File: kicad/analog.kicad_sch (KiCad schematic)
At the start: 61 parts, among them U1 MP2672GD-0000-Z, U3 MP2236CGJ-Z, U5 MP2672GD-0000-Z, U6 MP2236CGJ-P, U7 MP2236CGJ-P

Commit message: delete trailing space
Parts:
- U1: LCSC PN (none) -> C2837210; LCSC PN  C2837210 -> (none)
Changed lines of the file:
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@@
 			)
 		)
-		(property "LCSC PN " "C2837210"
+		(property "LCSC PN" "C2837210"
 			(at 180.848 27.178 0)
 			(effects

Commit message: update anotations
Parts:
- removed C1, C4, C5, C6, C9: 22u, Capacitor_SMD:C_0402_1005Metric, symbol Device:C
- removed C12, C13, C17, C18, C19, C22: 22u, Capacitor_SMD:C_0805_2012Metric, symbol Device:C
- removed C14: 1u, Capacitor_SMD:C_0805_2012Metric, symbol Device:C
- removed C15, C23: 1u, Capacitor_SMD:C_0603_1608Metric, symbol Device:C
- removed C16: 0.1u, Capacitor_SMD:C_0603_1608Metric, symbol Device:C
- removed C2: 220p, Capacitor_SMD:C_0402_1005Metric, symbol Device:C
- removed C20: 220p, Capacitor_SMD:C_0603_1608Metric, symbol Device:C
- removed C21: 10u, Capacitor_SMD:C_0805_2012Metric, symbol Device:C
- removed C25: 22u, Capacitor_SMD:C_1206_3216Metric, symbol Device:C
- removed C26: 100n, Capacitor_SMD:C_0603_1608Metric, symbol Device:C
- removed C3: 0.1u, Capacitor_SMD:C_0402_1005Metric, symbol Device:C
- removed C7, C8: 1u, Capacitor_SMD:C_0402_1005Metric, symbol Device:C
- removed D4: LED, LED_SMD:LED_0603_1608Metric, symbol Device:LED
- removed L1: MPL-AL6050-3R3, POWERLIB:2-SMD, symbol Device:L
- removed L2: MPL-AL6050-2R2, POWERLIB:2-SMD, symbol Device:L
- removed L3: 1.5uH, POWERLIB:IND-SMD_L7.0-W6.6, symbol powermodule:MWSA0605S-1R5MT
- removed R10: 100k, Resistor_SMD:R_0402_1005Metric, symbol Device:R
- removed R11: 10R, Resistor_SMD:R_1206_3216Metric, symbol Device:R
- removed R13: 100k, Resistor_SMD:R_0603_1608Metric, symbol Device:R
- removed R14: 5.5k, Resistor_SMD:R_0603_1608Metric, symbol Device:R
- removed R15, R24: 100R, Resistor_SMD:R_0805_2012Metric, symbol Device:R
- removed R16: 30k, Resistor_SMD:R_0603_1608Metric, symbol Device:R
- removed R17, R23: 60R, Resistor_SMD:R_1206_3216Metric, symbol Device:R
- removed R18: 8k, Resistor_SMD:R_0603_1608Metric, symbol Device:R
- removed R19: 12.6k, Resistor_SMD:R_0603_1608Metric, symbol Device:R
- removed R20: 3.6k, Resistor_SMD:R_0603_1608Metric, symbol Device:R
- removed R21: 2k, Resistor_SMD:R_0603_1608Metric, symbol Device:R
- removed R22: NTCG103JF103FT1, Diode_SMD:D_0402_1005Metric, symbol powermodule:NTCG103JF103FT1
- removed R9: 13.7k, Resistor_SMD:R_0402_1005Metric, symbol Device:R
- removed U5: MP2672GD-0000-Z, POWERLIB:QFN-18_2MMx3MM_MP2672_MNP_MPS, symbol powermodule:MP2672GD-0000-Z
- removed U6, U7: MP2236CGJ-P, POWERLIB:TSOT23-8_MP2236C_MNP, symbol powermodule:MP2236CGJ-P
- added D2: LED, symbol Device:LED
- D3: footprint LED_SMD:LED_0603_1608Metric -> (none); JLC Link https://jlcpcb.com/partdetail/Hubei_KentoElec-KT0603R/C2286 -> (none); LCSC Part # C2286 -> (none); basic? yes -> (none); info Red LED -> (none); price C$0.0075 -> (none)
- R1: value 22.1k -> R; footprint Resistor_SMD:R_0603_1608Metric -> (none); basic? yes -> (none); info 22.1k ohm -> (none)
- R25: value R -> 30k
- R8: value 10R -> R; footprint Resistor_SMD:R_0402_1005Metric -> (none); basic? yes -> (none); info 10 ohm -> (none)
- U1: LCSC PN  (none) -> C2837210
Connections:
- net VBUS: now also D2.2 (A)
- net VCC: now also D3.2 (A); no longer U1.16 (*STAT), U1.18 (*ACOK)
- net VSYS: now reaches C29.1, U1.11 (SYS)
- net at R8.2: now also D3.1 (K)
- net at R8.1: now also U1.16 (*STAT)
- net FB2: no longer names the net of R1.2
- net FB2: now also D2.1 (K)
- net LOAD_GND: no longer names the net of R1.1
- net LOAD_GND: now also U1.18 (*ACOK)
- no-connect marks 3 -> 2
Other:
- note removed: "Charging and Balancing"
- note removed: "Step down 5v to 3.3v"
- note removed: "Step down 8.4v to 5v"
- moved on the sheet: C27, R5, R6, U1

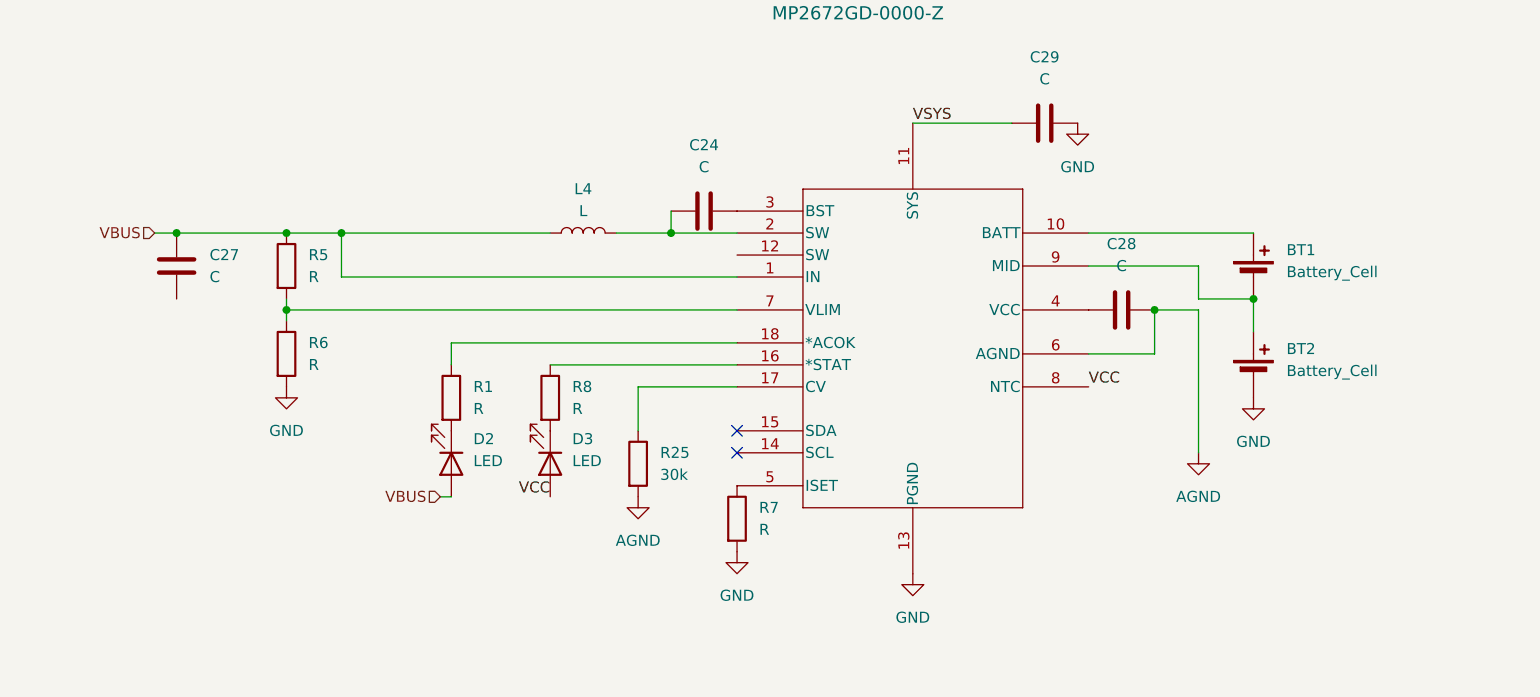
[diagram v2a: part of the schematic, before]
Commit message: add MB30 connector
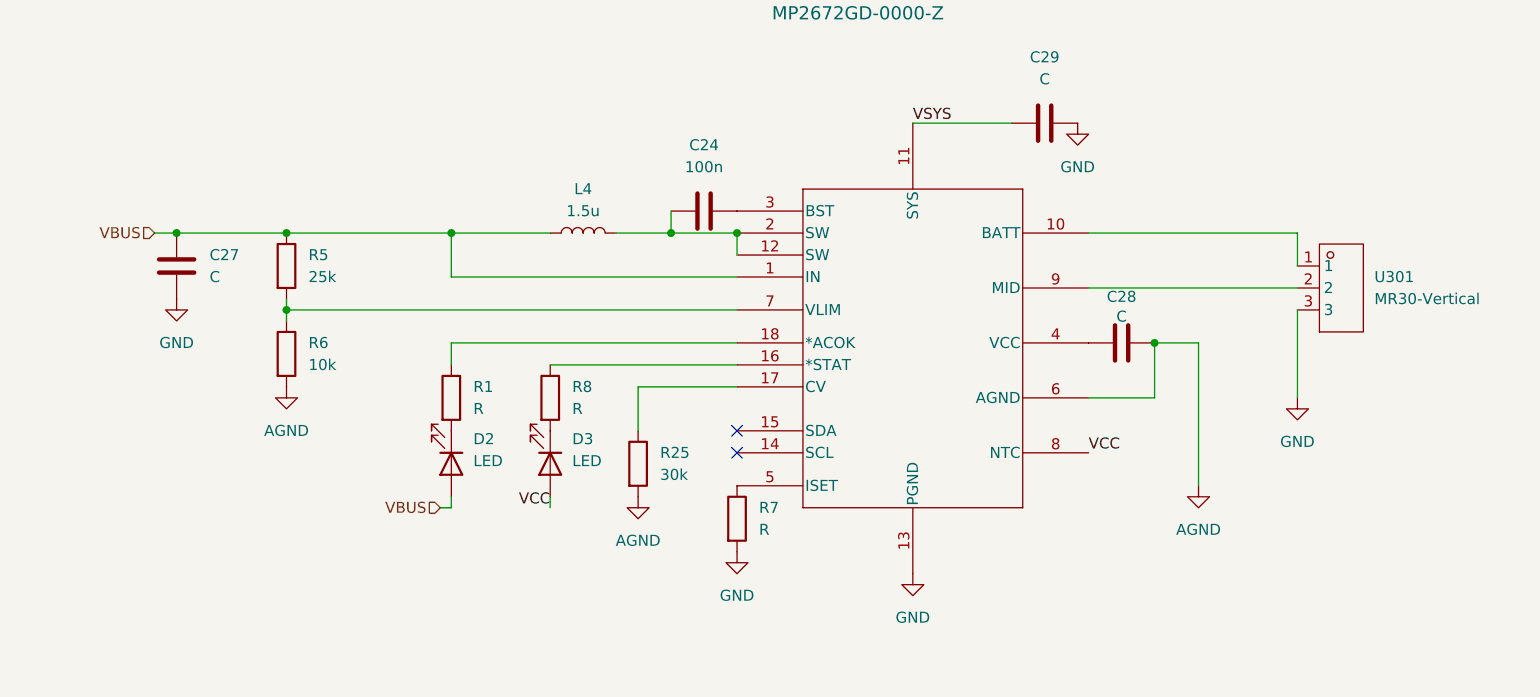
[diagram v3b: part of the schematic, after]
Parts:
- removed BT1, BT2: Battery_Cell, symbol Device:Battery_Cell
- added U301: MR30-Vertical, 4in-power:CONN-TH_MR30-Vertical, symbol 4in-power:MR30-Vertical
- C24: value C -> 100n
- L4: value L -> 1.5u
- R5: value R -> 25k
- R6: value R -> 10k
- U1: LCSC PN  C2837210 -> (none)
- U3: footprint TSOT23-8_MP2236C_MNP -> 4in-power:TSOT23-8_MP2236C_MNP
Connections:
- net AGND: now also R6.2
- net GND: now also C27.1, U301.3; no longer R6.2
- net at C24.1, L4.2, U1.2 (SW): now also U1.12 (SW)
- net at U1.10 (BATT): now also U301.1
- net at U1.9 (MID): now also U301.2
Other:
- moved on the sheet: C28

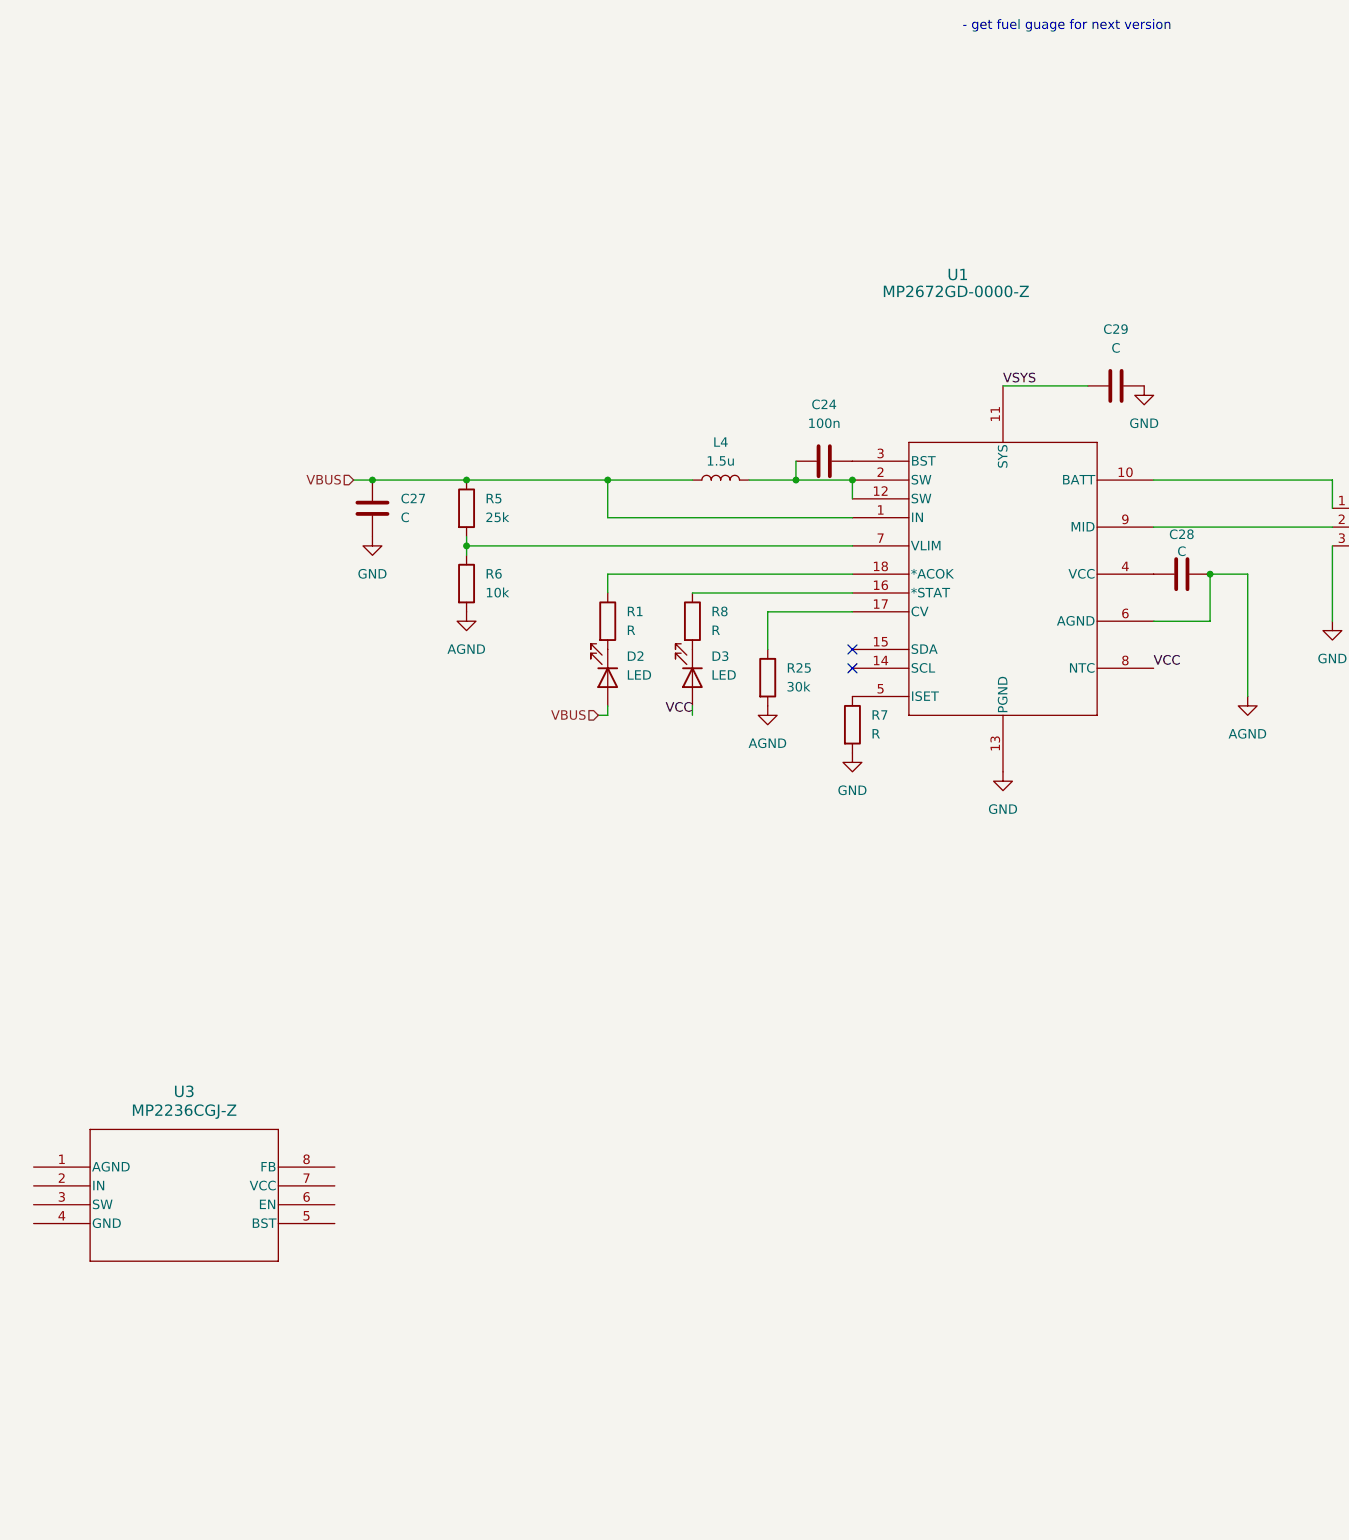
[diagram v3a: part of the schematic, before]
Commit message: update symbol data fields, add lcsc PN and links
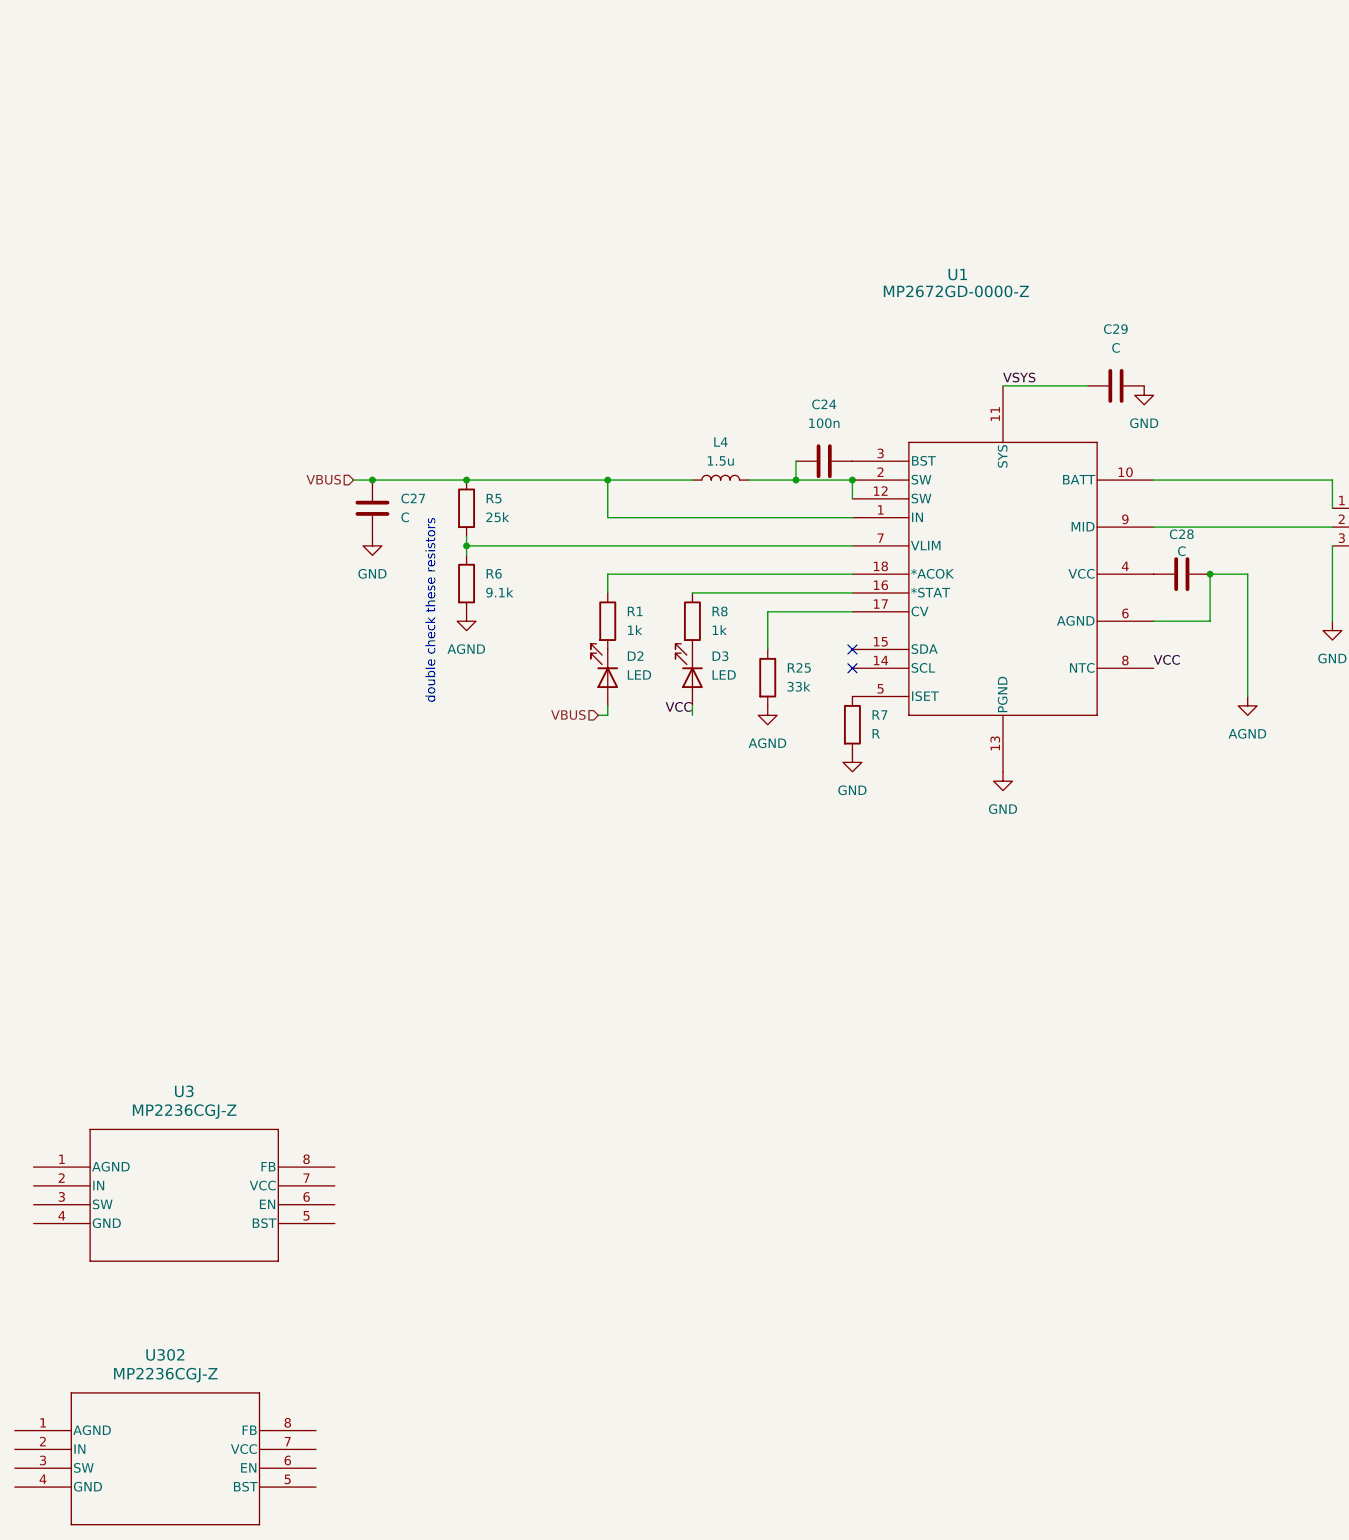
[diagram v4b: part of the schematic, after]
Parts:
- added U302: MP2236CGJ-Z, 4in-power:TSOT23-8_MP2236C_MNP, symbol 4in-power:MP2236CGJ-Z
- D2: footprint (none) -> LED_SMD:LED_0603_1608Metric; JLC Link (none) -> https://jlcpcb.com/partdetail/Hubei_KentoElec-KT0603B/C2288; LCSC PN (none) -> C2288
- D3: footprint (none) -> LED_SMD:LED_0603_1608Metric; JLC Link (none) -> https://jlcpcb.com/partdetail/Hubei_KentoElec-KT0603R/C2286; LCSC PN (none) -> C2286
- R1, R8: value R -> 1k
- R25: value 30k -> 33k
- R5: footprint (none) -> Resistor_SMD:R_0805_2012Metric
- R6: value 10k -> 9.1k; footprint (none) -> Resistor_SMD:R_0805_2012Metric; JLC Link (none) -> https://jlcpcb.com/partdetail/18543-0805W8F9101T5E/C17855; LCSC PN (none) -> C17855
- U1: DigKey Link https://www.digikey.ca/en/products/detail/monolithic-power-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 -> (none); Manufacturer PN MP2672GD-0000-P -> (none)
- U3: Manufacturer PN MP2236GJ-Z -> (none)
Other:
- note added: "double check these resistors"
- note removed: "- get fuel guage for next version"
